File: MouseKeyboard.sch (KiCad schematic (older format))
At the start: 15 parts

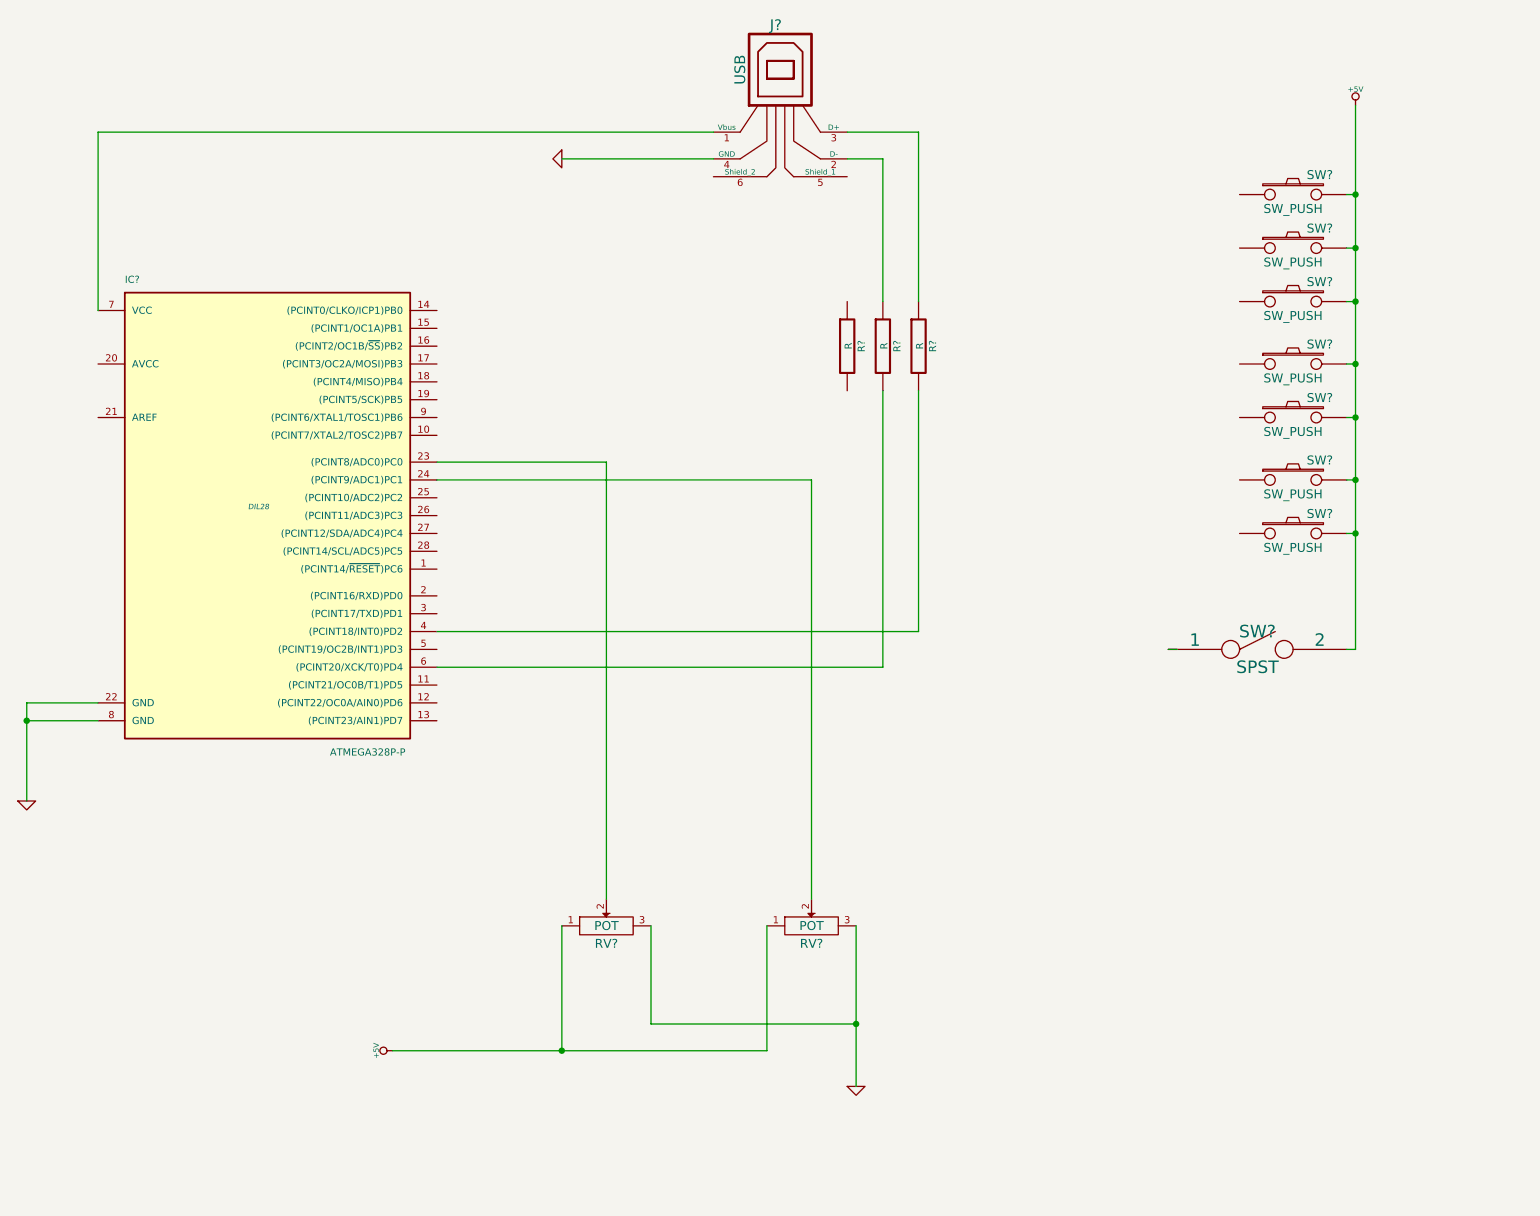
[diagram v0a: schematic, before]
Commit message: Replace Trinket With Pro-Trinket
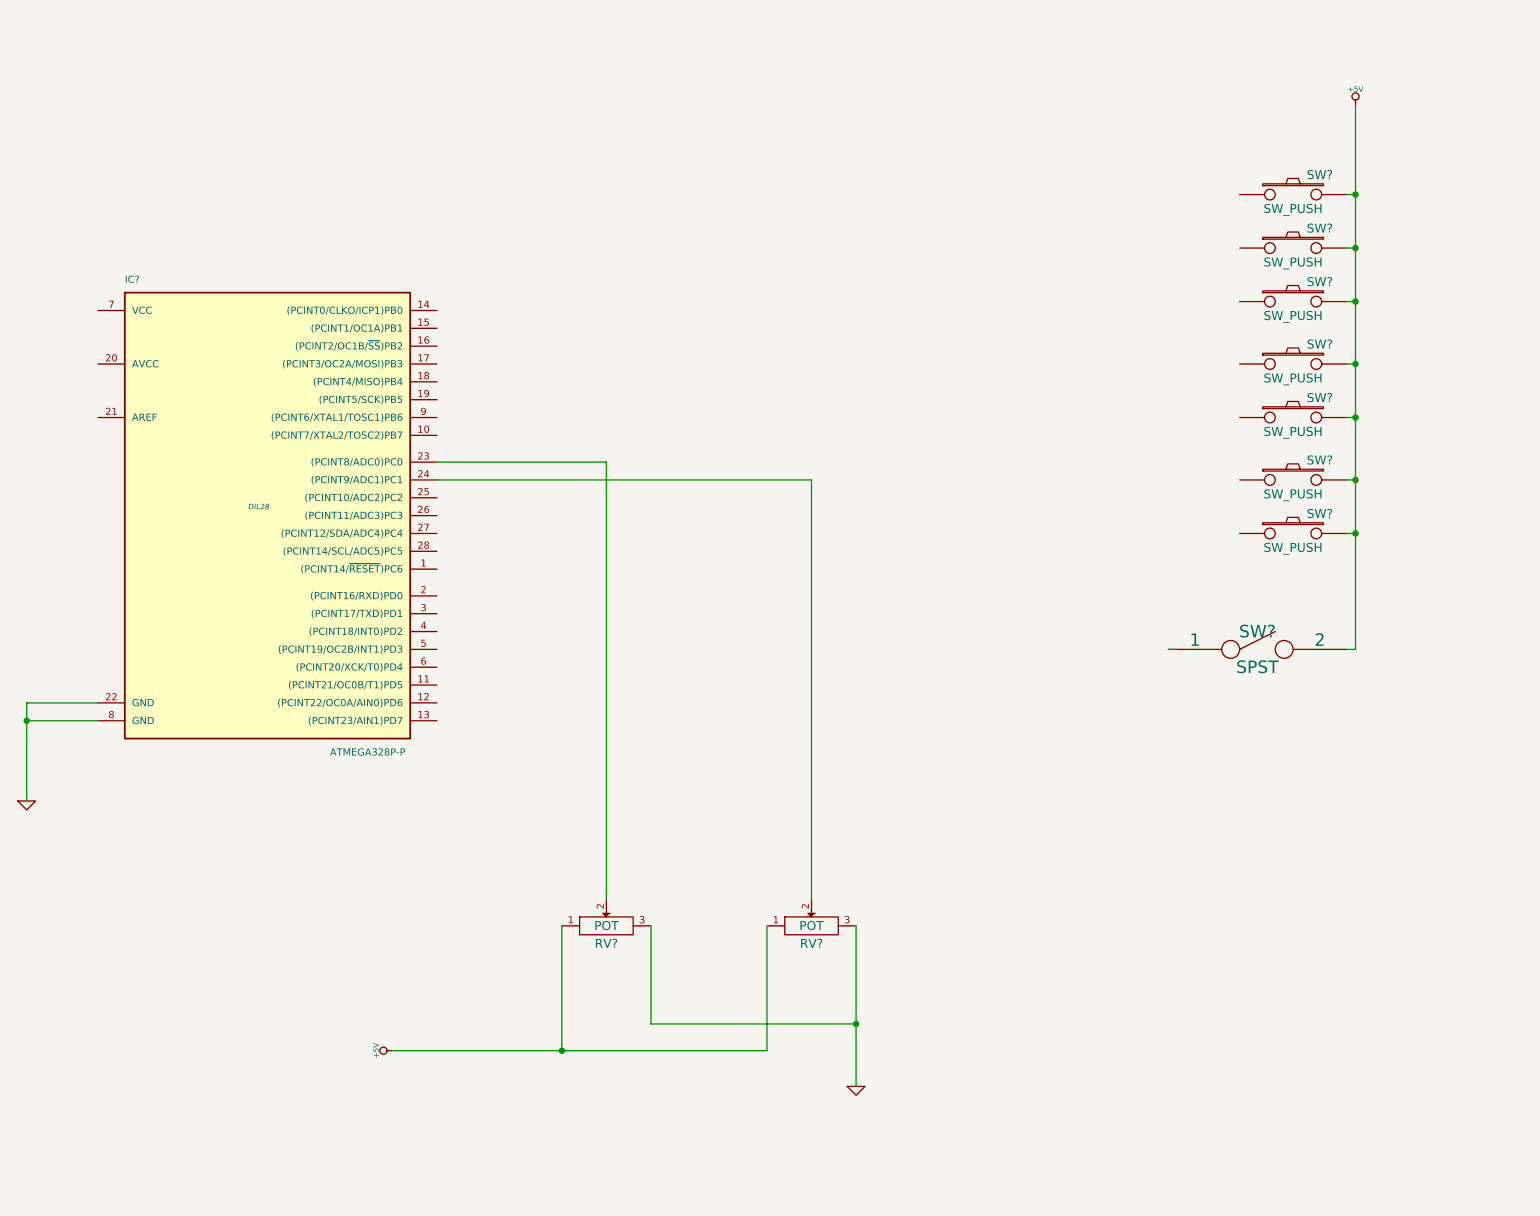
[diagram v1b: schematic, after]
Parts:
- removed J?: USB, symbol USB
- removed R? (x3): R, symbol R
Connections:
- wire segments 34 -> 23
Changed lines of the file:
@@
 Wire Wire Line
 	7600 4300 7650 4300
-$Comp
-L USB J?
-U 1 1 54DABFCC
-P 5450 1200
-F 0 "J?" H 5400 1600 60  0000 C CNN
-F 1 "USB" V 5200 1350 60  0000 C CNN
-F 2 "" H 5450 1200 60  0000 C CNN
-F 3 "" H 5450 1200 60  0000 C CNN
-	1    5450 1200
-	1    0    0    -1
-$EndComp
 Wire Wire Line
 	4450 5700 4450 3250
@@
 	1600 4600 1200 4600
 Connection ~ 1200 4700
-$Comp
-L GND #PWR?
-U 1 1 54DD41B3
-P 4200 1550
-F 0 "#PWR?" H 4200 1550 30  0001 C CNN
-F 1 "GND" H 4200 1480 30  0001 C CNN
-F 2 "" H 4200 1550 60  0000 C CNN
-F 3 "" H 4200 1550 60  0000 C CNN
-	1    4200 1550
-	0    1    1    0
-$EndComp
-Wire Wire Line
-	5050 1550 4200 1550
-$Comp
-L R R?
-U 1 1 54DD4896
-P 5800 2600
-F 0 "R?" V 5880 2600 40  0000 C CNN
-F 1 "R" V 5807 2601 40  0000 C CNN
-F 2 "" V 5730 2600 30  0000 C CNN
-F 3 "" H 5800 2600 30  0000 C CNN
-	1    5800 2600
-	1    0    0    -1
-$EndComp
-$Comp
-L R R?
-U 1 1 54DD48AA
-P 6000 2600
-F 0 "R?" V 6080 2600 40  0000 C CNN
-F 1 "R" V 6007 2601 40  0000 C CNN
-F 2 "" V 5930 2600 30  0000 C CNN
-F 3 "" H 6000 2600 30  0000 C CNN
-	1    6000 2600
-	1    0    0    -1
-$EndComp
-$Comp
-L R R?
-U 1 1 54DD48BE
-P 6200 2600
-F 0 "R?" V 6280 2600 40  0000 C CNN
-F 1 "R" V 6207 2601 40  0000 C CNN
-F 2 "" V 6130 2600 30  0000 C CNN
-F 3 "" H 6200 2600 30  0000 C CNN
-	1    6200 2600
-	1    0    0    -1
-$EndComp
-Wire Wire Line
-	5050 1400 1600 1400
-Wire Wire Line
-	1600 1400 1600 2400
-Wire Wire Line
-	3500 4200 6200 4200
-Wire Wire Line
-	6200 1400 5800 1400
-Wire Wire Line
-	6200 2350 6200 1400
-Wire Wire Line
-	6200 4200 6200 2850
-Wire Wire Line
-	5800 1550 6000 1550
-Wire Wire Line
-	6000 1550 6000 2350
-Wire Wire Line
-	3500 4400 6000 4400
-Wire Wire Line
-	6000 4400 6000 2850
 $EndSCHEMATC

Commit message: Constants
* Constants in header
* USB Schematic
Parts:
- added D? (x2): DIODESCH, symbol DIODESCH
- added J?: USB, symbol USB
- added R? (x3): R, symbol R
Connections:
- net labels added: Digital2, Digital7
- wire segments 23 -> 38
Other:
- moved on the sheet: SW?
